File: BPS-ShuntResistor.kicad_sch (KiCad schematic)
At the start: 14 parts, among them J1 Amp_Conn, J2 Test_V_In, J3 Test_V_Out

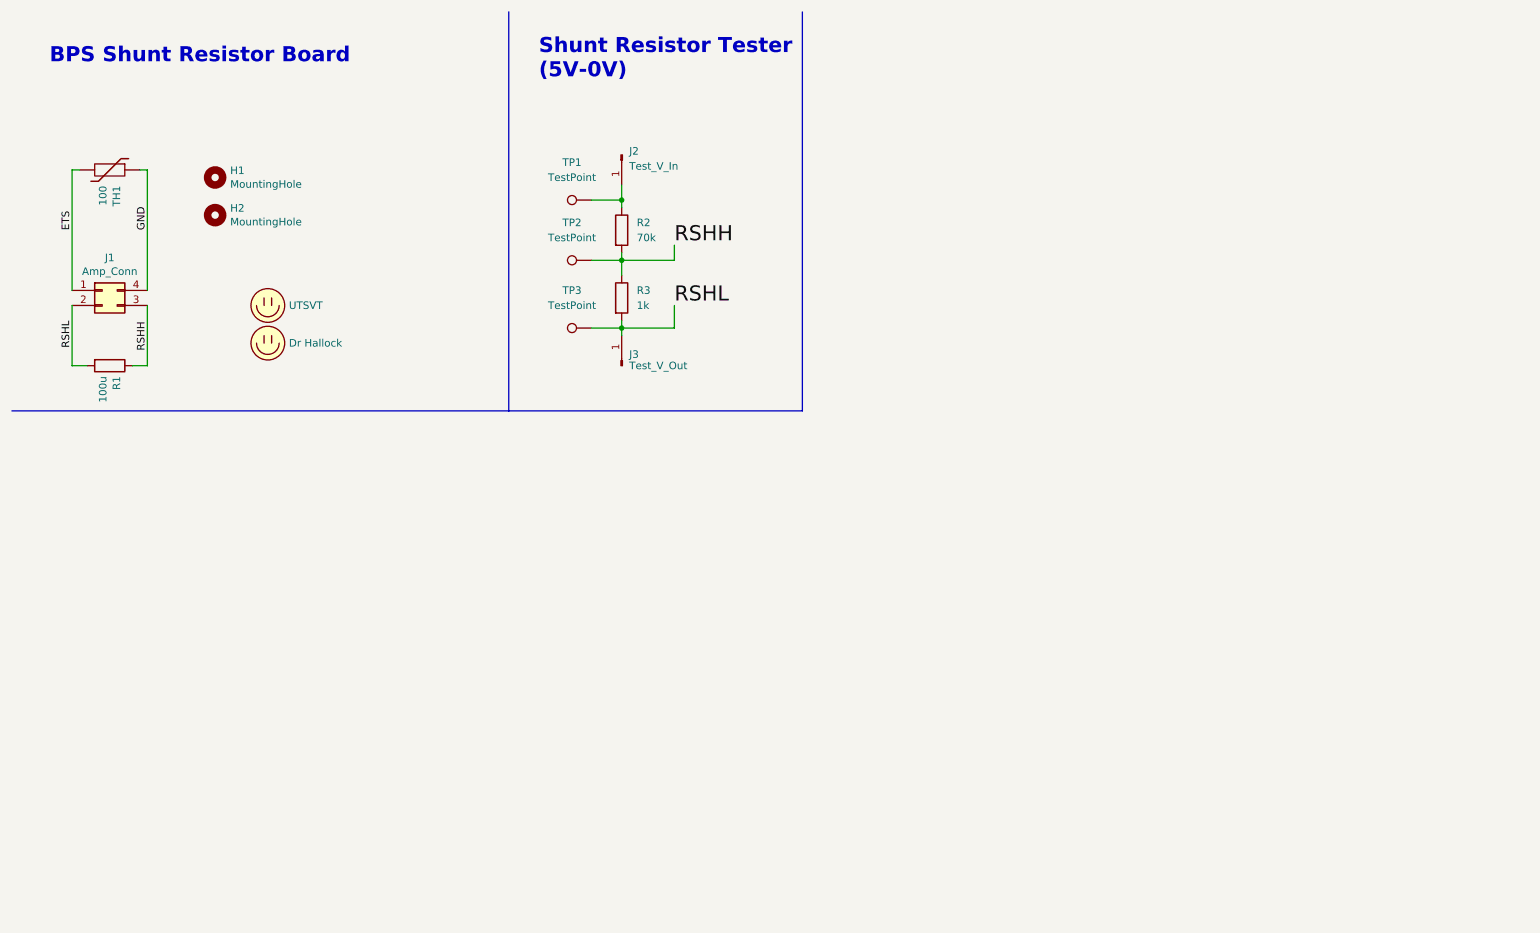
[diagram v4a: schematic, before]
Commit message: working on new board
connector for current board, testing for shunt
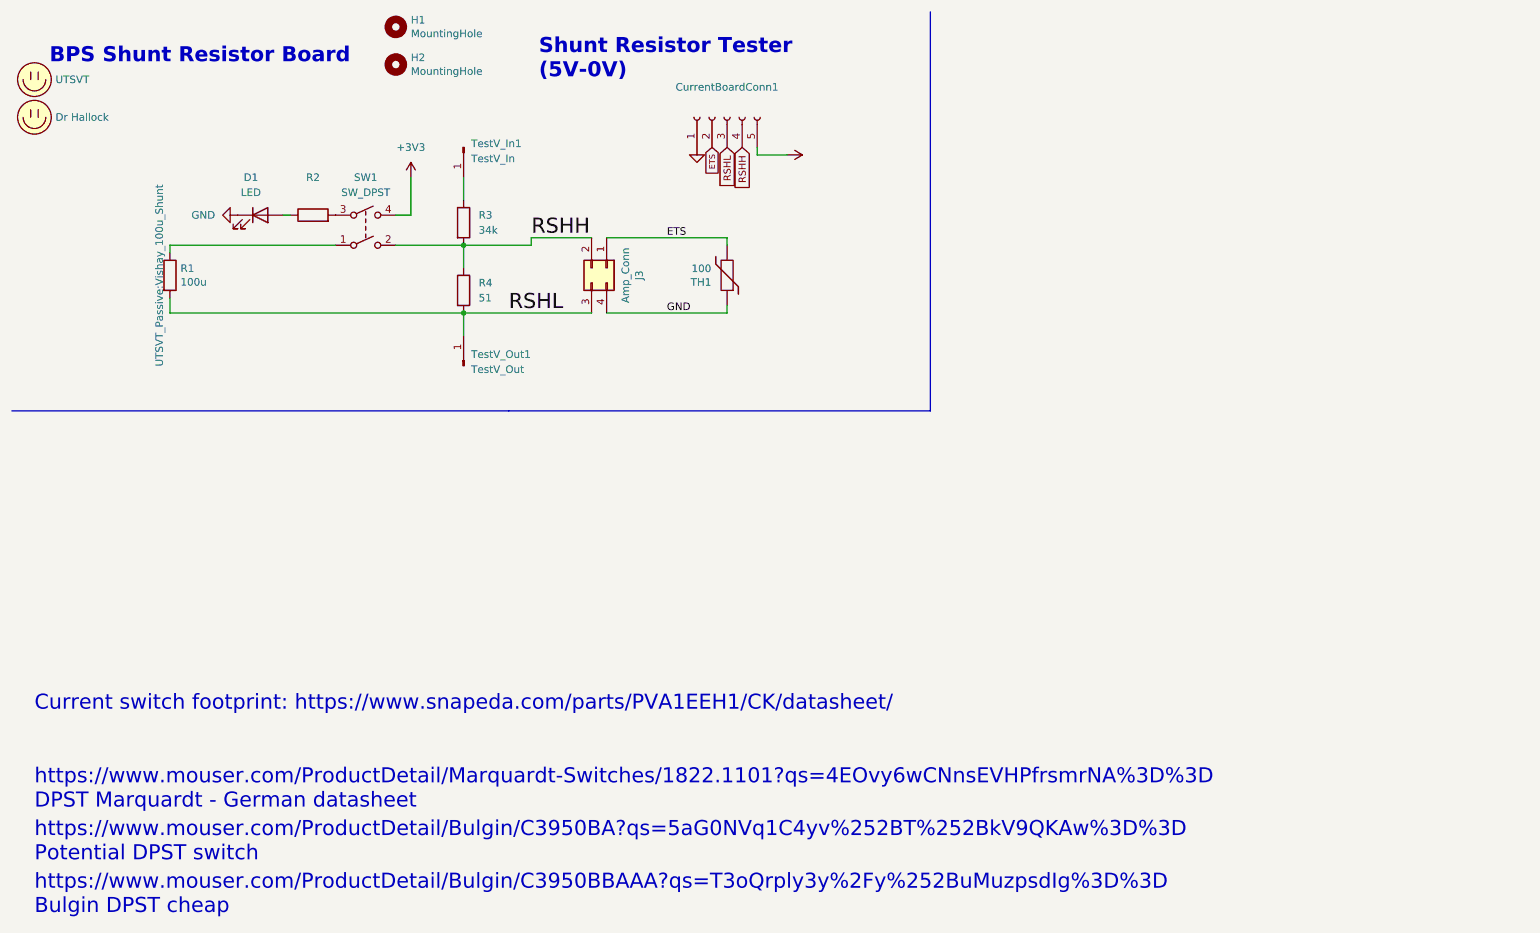
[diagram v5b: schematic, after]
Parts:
- removed J1: Amp_Conn, UTSVT_Connectors:Power_Metal_Strip_Battery_Shunt_Resistor_4_Pin_Connector, symbol Connector_Generic:Conn_02x02_Counter_Clockwise
- removed J2: Test_V_In, Connector_PinHeader_2.54mm:PinHeader_1x01_P2.54mm_Vertical, symbol Connector:Conn_01x01_Male
- removed J3: Test_V_Out, Connector_PinHeader_2.54mm:PinHeader_1x01_P2.54mm_Vertical, symbol Connector:Conn_01x01_Male
- removed TP1, TP2, TP3: TestPoint, TestPoint:TestPoint_Bridge_Pitch3.81mm_Drill1.3mm, symbol Connector:TestPoint
- added CurrentBoardConn1: (no value), symbol Connector:Conn_01x05_Female
- added D1: LED, LED_SMD:LED_0805_2012Metric, symbol Device:LED
- added J3: Amp_Conn, UTSVT_Connectors:Power_Metal_Strip_Battery_Shunt_Resistor_4_Pin_Connector, symbol Connector_Generic:Conn_02x02_Counter_Clockwise
- added R4: 51, Resistor_SMD:R_0805_2012Metric, symbol Device:R
- added SW1: SW_DPST, UTSVT_Passive:SW_PVA1EEH1, symbol Switch:SW_DPST
- added TestV_In1: TestV_In, Connector_PinSocket_2.54mm:PinSocket_1x01_P2.54mm_Vertical, symbol Connector:Conn_01x01_Male
- added TestV_Out1: TestV_Out, Connector_PinSocket_2.54mm:PinSocket_1x01_P2.54mm_Vertical, symbol Connector:Conn_01x01_Male
- R1: footprint UTSVT_Passive:Vishay_Shunt_Resistor_100u -> UTSVT_Passive:Vishay_100u_Shunt
- R2: value 70k -> (none)
- R3: value 1k -> 34k
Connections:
- net ETS: now also CurrentBoardConn1.2 (Pin_2), J3.1 (Pin_1)
- net GND: now also CurrentBoardConn1.1 (Pin_1), D1.1 (K), J3.4 (Pin_4)
- net RSHH: now also R3.2, CurrentBoardConn1.4 (Pin_4), J3.2 (Pin_2), R4.1, SW1.2; no longer R1.1, R2.2, R3.1
- net RSHL: now also CurrentBoardConn1.3 (Pin_3), J3.3 (Pin_3), R4.2, TestV_Out1.1 (Pin_1); no longer R3.2
- net at R2.1: now also D1.2 (A)
- new net: R1.1, SW1.1
- new net: R2.2, SW1.3
- new net: R3.1, TestV_In1.1 (Pin_1)
- new net +3V3: CurrentBoardConn1.5 (Pin_5), SW1.4
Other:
- note added: "Current switch footprint: https://www.snapeda.com/parts/PVA1EEH1/CK/datasheet/"
- note added: "https://www.mouser.com/ProductDetail/Bulgin/C3950BA?qs=5aG0NVq1C4yv%252BT%252BkV9QKAw%3D%3D Potential DPST switch"
- note added: "https://www.mouser.com/ProductDetail/Bulgin/C3950BBAAA?qs=T3oQrply3y%2Fy%252BuMuzpsdIg%3D%3D Bulgin DPST cheap"
- note added: "https://www.mouser.com/ProductDetail/Marquardt-Switches/1822.1101?qs=4EOvy6wCNnsEVHPfrsmrNA%3D%3D DPST Marquardt - German datasheet"
- moved on the sheet: H1, H2, R1

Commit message: pcb v1 not done
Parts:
- CurrentBoardConn1: value (none) -> Conn_01x05_Female; footprint (none) -> Connector_PinSocket_2.54mm:PinSocket_1x05_P2.54mm_Vertical_SMD_Pin1Right
- R2: value (none) -> 1.6k
- TestV_In1, TestV_Out1: footprint Connector_PinSocket_2.54mm:PinSocket_1x01_P2.54mm_Vertical -> (none)
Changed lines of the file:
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@@
       (effects (font (size 1.27 1.27)) (justify right))
     )
-    (property "Footprint" "Connector_PinSocket_2.54mm:PinSocket_1x01_P2.54mm_Vertical" (id 2) (at 88.9 72.39 0)
+    (property "Footprint" "" (id 2) (at 88.9 72.39 0)
       (effects (font (size 1.27 1.27)) hide)
     )
@@
     (in_bom yes) (on_board yes) (fields_autoplaced)
     (property "Reference" "R2" (id 0) (at 63.5 40.64 90))
-    (property "Value" "" (id 1) (at 63.5 43.18 90))
+    (property "Value" "1.6k" (id 1) (at 63.5 43.18 90))
     (property "Footprint" "Resistor_SMD:R_0805_2012Metric" (id 2) (at 63.5 48.768 90)
       (effects (font (size 1.27 1.27)) hide)
@@
     (in_bom yes) (on_board yes) (fields_autoplaced)
     (property "Reference" "CurrentBoardConn1" (id 0) (at 133.35 25.4 90))
-    (property "Value" "" (id 1) (at 133.35 27.94 90))
-    (property "Footprint" "" (id 2) (at 133.35 30.48 0)
+    (property "Value" "Conn_01x05_Female" (id 1) (at 133.35 27.94 90))
+    (property "Footprint" "Connector_PinSocket_2.54mm:PinSocket_1x05_P2.54mm_Vertical_SMD_Pin1Right" (id 2) (at 133.35 30.48 0)
       (effects (font (size 1.27 1.27)) hide)
     )
@@
       (effects (font (size 1.27 1.27)) hide)
     )
-    (property "Value" "" (id 1) (at 128.27 40.64 0))
+    (property "Value" "GND" (id 1) (at 128.27 40.64 0))
     (property "Footprint" "" (id 2) (at 128.27 35.56 0)
       (effects (font (size 1.27 1.27)) hide)
@@
       (effects (font (size 1.27 1.27)) (justify left))
     )
-    (property "Footprint" "Connector_PinSocket_2.54mm:PinSocket_1x01_P2.54mm_Vertical" (id 2) (at 88.9 35.56 0)
+    (property "Footprint" "" (id 2) (at 88.9 35.56 0)
       (effects (font (size 1.27 1.27)) hide)
     )
@@
       (effects (font (size 1.27 1.27)) hide)
     )
-    (property "Value" "" (id 1) (at 147.32 36.8299 90)
+    (property "Value" "+3V3" (id 1) (at 147.32 36.8299 90)
       (effects (font (size 1.27 1.27)) (justify left))
     )
@@
     )
     (path "/84a7fc7b-5bd9-45c8-89b5-3a5bcad31a54"
-      (reference "TestV_In1") (unit 1) (value "TestV_In") (footprint "Connector_PinSocket_2.54mm:PinSocket_1x01_P2.54mm_Vertical")
+      (reference "TestV_In1") (unit 1) (value "TestV_In") (footprint "Connector_PinHeader_2.54mm:PinHeader_1x01_P2.54mm_Vertical")
     )
     (path "/269dc11e-3732-4b0d-8804-d7467b2caa7b"
-      (reference "TestV_Out1") (unit 1) (value "TestV_Out") (footprint "Connector_PinSocket_2.54mm:PinSocket_1x01_P2.54mm_Vertical")
-    )
-  )
+      (reference "TestV_Out1") (unit 1) (value "TestV_Out") (footprint "Connector_PinHeader_2.54mm:PinHeader_1x01_P2.54mm_Vertical")
+    )
+  )

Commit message: added more info per manthan
might need more changes
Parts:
- CurrentBoardConn1: footprint Connector_PinSocket_2.54mm:PinSocket_1x05_P2.54mm_Vertical_SMD_Pin1Right -> Connector_PinSocket_2.54mm:PinSocket_1x05_P2.54mm_Vertical
- TestV_In1: value TestV_In -> (none); footprint (none) -> Connector_PinHeader_2.54mm:PinHeader_1x01_P2.54mm_Vertical
- TestV_Out1: value TestV_Out -> (none); footprint (none) -> Connector_PinHeader_2.54mm:PinHeader_1x01_P2.54mm_Vertical
- renumbered SW1 to LED_BATT_Switch1
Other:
- note added: "+ -"
- note added: "BPS Shunt Resistor Board w/ tester"
- note added: "Divided Voltage"
- note added: "I_Batt <<"
- note added: "I_Batt >>"
- note removed: "BPS Shunt Resistor Board"
- note removed: "Current switch footprint: https://www.snapeda.com/parts/PVA1EEH1/CK/datasheet/"
- note removed: "Shunt Resistor Tester (5V-0V)"
- note removed: "https://www.mouser.com/ProductDetail/Bulgin/C3950BA?qs=5aG0NVq1C4yv%252BT%252BkV9QKAw%3D%3D Potential DPST switch"
- note removed: "https://www.mouser.com/ProductDetail/Bulgin/C3950BBAAA?qs=T3oQrply3y%2Fy%252BuMuzpsdIg%3D%3D Bulgin DPST cheap"
- note removed: "https://www.mouser.com/ProductDetail/Marquardt-Switches/1822.1101?qs=4EOvy6wCNnsEVHPfrsmrNA%3D%3D DPST Marquardt - German datasheet"
- moved on the sheet: CurrentBoardConn1, D1, H1, H2, J3, LED_BATT_Switch1, R1, R2, R3, R4, TH1, TestV_In1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

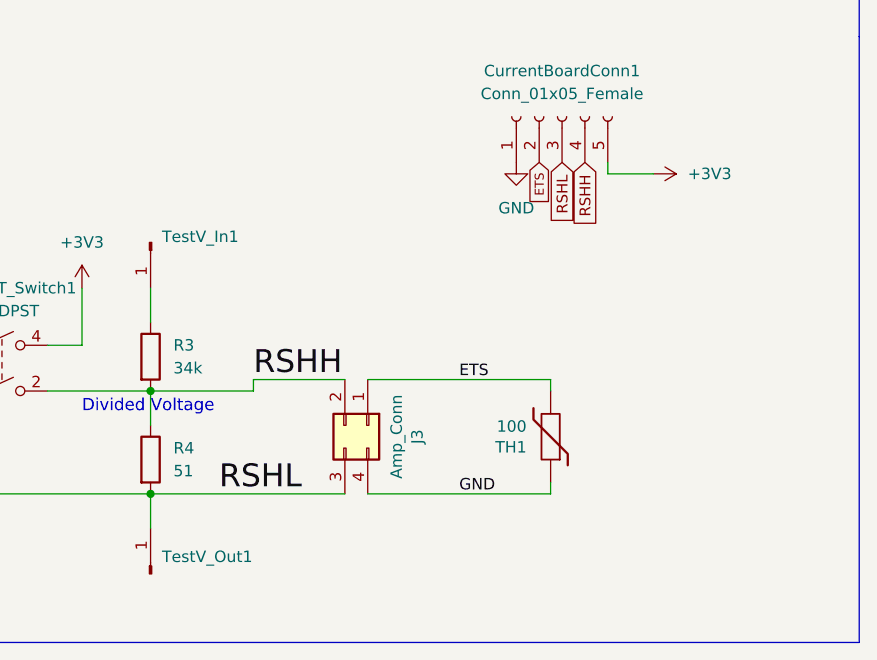
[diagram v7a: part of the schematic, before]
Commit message: Adjusting shunt-current connector pins
Tianda and I haven't really decided on footprint stuff yet but pins now line up.
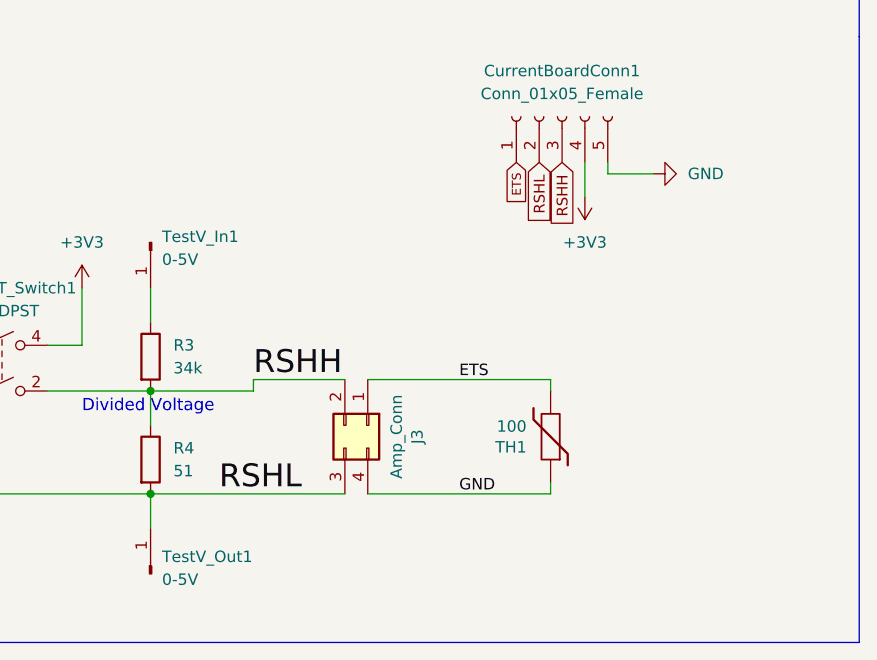
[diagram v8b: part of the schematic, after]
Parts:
- TestV_In1, TestV_Out1: value (none) -> 0-5V
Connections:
- net +3V3: now also CurrentBoardConn1.4 (Pin_4); no longer CurrentBoardConn1.5 (Pin_5)
- net ETS: now also CurrentBoardConn1.1 (Pin_1); no longer CurrentBoardConn1.2 (Pin_2)
- net GND: now also CurrentBoardConn1.5 (Pin_5); no longer CurrentBoardConn1.1 (Pin_1)
- net RSHH: now also CurrentBoardConn1.3 (Pin_3); no longer CurrentBoardConn1.4 (Pin_4)
- net RSHL: now also CurrentBoardConn1.2 (Pin_2); no longer CurrentBoardConn1.3 (Pin_3)
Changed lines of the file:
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@@
+    (stroke (width 0) (type default) (color 0 0 0 0))
+  )
+  (wire (pts (xy 201.93 85.09) (xy 201.93 81.28))
     (stroke (width 0) (type default) (color 0 0 0 0))
   )
@@
     (effects (font (size 2.54 2.54)) (justify left bottom))
   )
-  (global_label "RSHL" (shape input) (at 199.39 81.28 270) (fields_autoplaced)
+  (global_label "RSHL" (shape input) (at 196.85 81.28 270) (fields_autoplaced)
     (effects (font (size 1.2 1.2)) (justify right))
-    (property "Intersheet References" "${INTERSHEET_REFS}" (id 0) (at 199.315 88.0474 90)
+    (property "Intersheet References" "${INTERSHEET_REFS}" (id 0) (at 196.775 88.0474 90)
       (effects (font (size 1.2 1.2)) (justify right) hide)
     )
   )
-  (global_label "ETS" (shape input) (at 196.85 81.28 270) (fields_autoplaced)
+  (global_label "ETS" (shape input) (at 194.31 81.28 270) (fields_autoplaced)
     (effects (font (size 1 1)) (justify right))
-    (property "Intersheet References" "${INTERSHEET_REFS}" (id 0) (at 196.7875 85.729 90)
+    (property "Intersheet References" "${INTERSHEET_REFS}" (id 0) (at 194.2475 85.729 90)
       (effects (font (size 1 1)) (justify right) hide)
     )
   )
-  (global_label "RSHH" (shape input) (at 201.93 81.28 270) (fields_autoplaced)
+  (global_label "RSHH" (shape input) (at 199.39 81.28 270) (fields_autoplaced)
     (effects (font (size 1.2 1.2)) (justify right))
-    (property "Intersheet References" "${INTERSHEET_REFS}" (id 0) (at 201.855 88.3331 90)
+    (property "Intersheet References" "${INTERSHEET_REFS}" (id 0) (at 199.315 88.3331 90)
       (effects (font (size 1.2 1.2)) (justify right) hide)
     )
@@
       (effects (font (size 1.27 1.27)) (justify right))
     )
-    (property "Value" "" (id 1) (at 154.94 127.6349 90)
+    (property "Value" "0-5V" (id 1) (at 154.94 127.6349 90)
       (effects (font (size 1.27 1.27)) (justify right))
     )
@@
     (pin "4")
   )
-  (symbol (lib_id "power:GND") (at 194.31 81.28 0) (unit 1)
-    (in_bom yes) (on_board yes) (fields_autoplaced)
-    (property "Reference" "#PWR03" (id 0) (at 194.31 87.63 0)
-      (effects (font (size 1.27 1.27)) hide)
-    )
-    (property "Value" "GND" (id 1) (at 194.31 86.36 0))
-    (property "Footprint" "" (id 2) (at 194.31 81.28 0)
-      (effects (font (size 1.27 1.27)) hide)
-    )
-    (property "Datasheet" "" (id 3) (at 194.31 81.28 0)
+  (symbol (lib_id "power:GND") (at 209.55 82.55 90) (unit 1)
+    (in_bom yes) (on_board yes) (fields_autoplaced)
+    (property "Reference" "#PWR03" (id 0) (at 215.9 82.55 0)
+      (effects (font (size 1.27 1.27)) hide)
+    )
+    (property "Value" "GND" (id 1) (at 213.36 82.5499 90)
+      (effects (font (size 1.27 1.27)) (justify right))
+    )
+    (property "Footprint" "" (id 2) (at 209.55 82.55 0)
+      (effects (font (size 1.27 1.27)) hide)
+    )
+    (property "Datasheet" "" (id 3) (at 209.55 82.55 0)
       (effects (font (size 1.27 1.27)) hide)
     )
@@
       (effects (font (size 1.27 1.27)) (justify left))
     )
-    (property "Value" "" (id 1) (at 154.94 92.0749 90)
+    (property "Value" "0-5V" (id 1) (at 154.94 92.0749 90)
       (effects (font (size 1.27 1.27)) (justify left))
     )
@@
     (pin "1")
   )
-  (symbol (lib_id "power:+3V3") (at 209.55 82.55 270) (unit 1)
-    (in_bom yes) (on_board yes) (fields_autoplaced)
-    (property "Reference" "#PWR04" (id 0) (at 205.74 82.55 0)
-      (effects (font (size 1.27 1.27)) hide)
-    )
-    (property "Value" "+3V3" (id 1) (at 213.36 82.5499 90)
-      (effects (font (size 1.27 1.27)) (justify left))
-    )
-    (property "Footprint" "" (id 2) (at 209.55 82.55 0)
-      (effects (font (size 1.27 1.27)) hide)
-    )
-    (property "Datasheet" "" (id 3) (at 209.55 82.55 0)
-      (effects (font (size 1.27 1.27)) hide)
-    )
+  (symbol (lib_id "power:+3V3") (at 201.93 85.09 180) (unit 1)
+    (in_bom yes) (on_board yes) (fields_autoplaced)
+    (property "Reference" "#PWR04" (id 0) (at 201.93 81.28 0)
+      (effects (font (size 1.27 1.27)) hide)
+    )
+    (property "Value" "+3V3" (id 1) (at 201.93 90.17 0))
+    (property "Footprint" "" (id 2) (at 201.93 85.09 0)
+      (effects (font (size 1.27 1.27)) hide)
+    )
+    (property "Datasheet" "" (id 3) (at 201.93 85.09 0)
+      (effects (font (size 1.27 1.27)) hide)
+    )
